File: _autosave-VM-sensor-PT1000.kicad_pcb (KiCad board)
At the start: 2 copper layers, 25.4 x 21.6 mm, 17 parts, among them P1 PT100, P2 ADC, P3 PWR, U1 AMS1117, U2 MCP6001

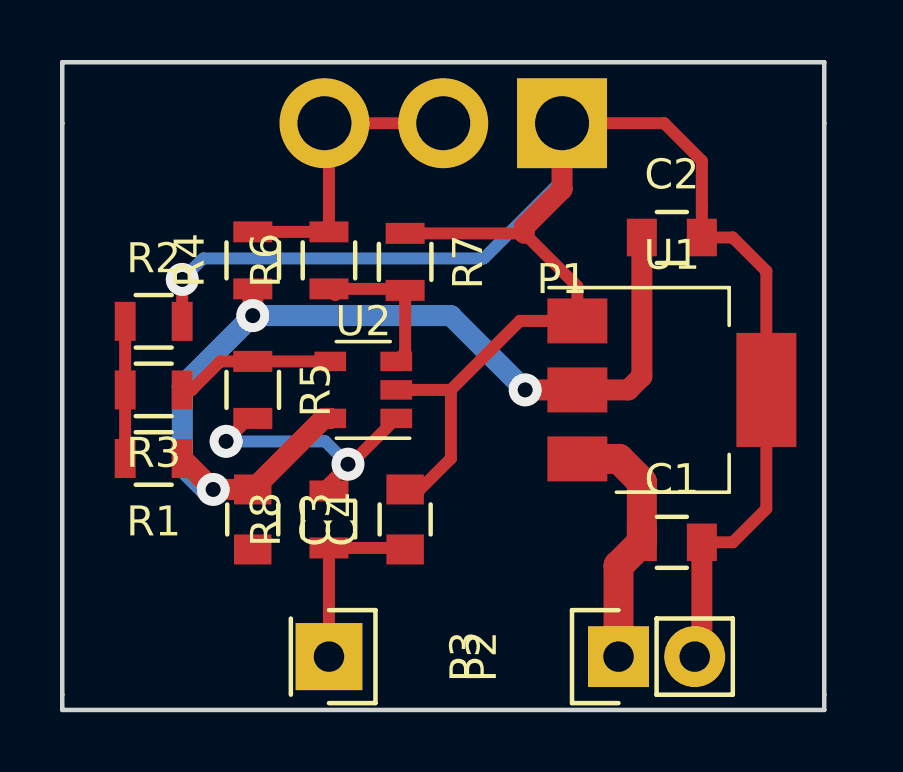
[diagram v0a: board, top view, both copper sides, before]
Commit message: change component 0603 to 0805 & header
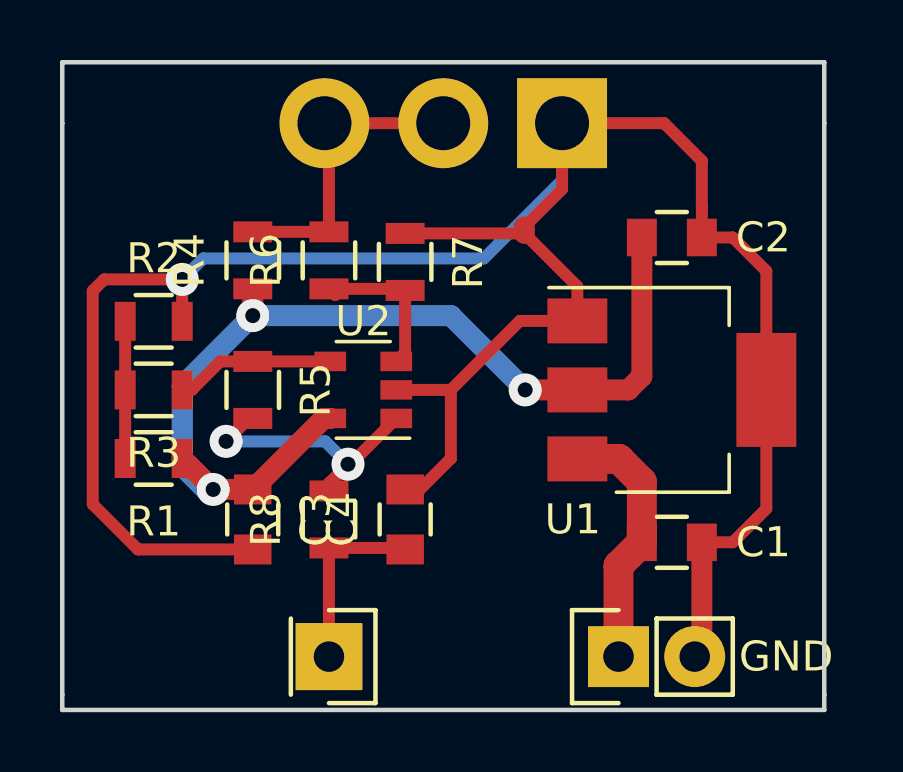
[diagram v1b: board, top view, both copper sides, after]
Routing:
- net GND: track 65.4 -> 81.6 mm
- added copper zone on B.Cu, net GND
- added copper zone on F.Cu, net GND
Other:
- board text added: "GND"
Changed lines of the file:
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@@
   (general
     (links 30)
-    (no_connects 5)
+    (no_connects 0)
     (area 114.224999 61.392999 139.775001 83.133001)
     (thickness 1.6)
-    (drawings 8)
-    (tracks 83)
+    (drawings 9)
+    (tracks 88)
     (zones 0)
     (modules 17)
@@
     (last_trace_width 0.4)
     (trace_clearance 0.2)
-    (zone_clearance 0.508)
+    (zone_clearance 0.4)
     (zone_45_only no)
     (trace_min 0.2)
@@
     (uvia_min_drill 0.1)
     (pcb_text_width 0.3)
-    (pcb_text_size 1.5 1.5)
+    (pcb_text_size 1 1)
     (mod_edge_width 0.15)
     (mod_text_size 1 1)
@@
     (descr "Hirose DF63 connector, DF63-3P-3.96DSA, 3.96mm pitch, top entry THT")
     (tags "connector hirose df63 vertical through hole")
-    (fp_text reference P1 (at 0 -5.2 180) (layer F.SilkS)
+    (fp_text reference P1 (at 0 -5.2 180) (layer F.SilkS) hide
       (effects (font (size 1 1) (thickness 0.15)))
     )
@@
     (tags "CMS SOT")
     (attr smd)
-    (fp_text reference U1 (at 0 -4.5) (layer F.SilkS)
+    (fp_text reference U1 (at -3.302 4.318) (layer F.SilkS)
       (effects (font (size 1 1) (thickness 0.15)))
     )
@@
     (tags "capacitor 0805")
     (attr smd)
-    (fp_text reference C1 (at 0 -2.1) (layer F.SilkS)
+    (fp_text reference C1 (at 3.048 0) (layer F.SilkS)
       (effects (font (size 1 1) (thickness 0.15)))
     )
@@
     (tags "capacitor 0805")
     (attr smd)
-    (fp_text reference C2 (at 0 -2.1) (layer F.SilkS)
+    (fp_text reference C2 (at 3.048 0) (layer F.SilkS)
       (effects (font (size 1 1) (thickness 0.15)))
     )
@@
     (descr "Through hole pin header")
     (tags "pin header")
-    (fp_text reference P3 (at 0 -5.1 90) (layer F.SilkS)
+    (fp_text reference P3 (at 0 -5.1 90) (layer F.SilkS) hide
       (effects (font (size 1 1) (thickness 0.15)))
     )
@@
     (descr "Through hole pin header")
     (tags "pin header")
-    (fp_text reference P2 (at 0 -5.1 270) (layer F.SilkS)
+    (fp_text reference P2 (at 0 -5.1 270) (layer F.SilkS) hide
       (effects (font (size 1 1) (thickness 0.15)))
     )
@@
       (rotate (xyz 0 0 90))
     )
+  )
+  (gr_text GND (at 138.43 81.28) (layer F.SilkS)
+    (effects (font (size 1 1) (thickness 0.25)))
   )
   (gr_line (start 139.7 61.468) (end 139.7 63.5) (layer Edge.Cuts) (width 0.15))
@@
   (segment (start 133.62 77.47) (end 132.842 78.248) (width 1) (layer F.Cu) (net 1))
   (segment (start 132.842 78.248) (end 132.842 81.28) (width 1) (layer F.Cu) (net 1))
+  (segment (start 120.65 77.708) (end 116.824 77.708) (width 0.4) (layer F.Cu) (net 2))
+  (segment (start 116.824 77.708) (end 115.316 76.2) (width 0.4) (layer F.Cu) (net 2))
+  (segment (start 115.316 76.2) (end 115.316 69.088) (width 0.4) (layer F.Cu) (net 2))
+  (segment (start 115.316 69.088) (end 115.697 68.707) (width 0.4) (layer F.Cu) (net 2))
+  (segment (start 115.697 68.707) (end 118.3005 68.707) (width 0.4) (layer F.Cu) (net 2))
   (segment (start 118.999 68.0085) (end 128.3515 68.0085) (width 0.4) (layer B.Cu) (net 2))
   (segment (start 128.3515 68.0085) (end 130.96 65.4) (width 0.4) (layer B.Cu) (net 2))
@@
   (segment (start 136.652 77.47) (end 137.77 76.352) (width 0.4) (layer F.Cu) (net 2))
   (segment (start 137.77 76.352) (end 137.77 72.39) (width 0.4) (layer F.Cu) (net 2))
-  (segment (start 130.96 63.5) (end 130.96 65.7) (width 0.7) (layer F.Cu) (net 2))
-  (segment (start 130.96 65.7) (end 129.7028 66.9572) (width 0.7) (layer F.Cu) (net 2))
+  (segment (start 130.96 63.5) (end 130.96 65.7) (width 0.4) (layer F.Cu) (net 2))
+  (segment (start 130.96 65.7) (end 129.7028 66.9572) (width 0.4) (layer F.Cu) (net 2))
   (segment (start 129.7028 66.9572) (end 129.7028 67.1728) (width 0.7) (layer F.Cu) (net 2))
   (segment (start 130.96 63.5) (end 134.366 63.5) (width 0.4) (layer F.Cu) (net 2))
@@
   (segment (start 123.19 69.022) (end 125.6792 69.022) (width 0.4) (layer F.Cu) (net 9))
   (segment (start 125.6792 69.022) (end 125.73 69.0728) (width 0.4) (layer F.Cu) (net 9))
+  (zone (net 2) (net_name GND) (layer F.Cu) (hatch edge 0.508)
+    (connect_pads (clearance 0.4))
+    (min_thickness 0.4)
+    (fill yes (arc_segments 32) (thermal_gap 0.508) (thermal_bridge_width 0.508))
+    (polygon
+      (pts
+        (xy 114.3 61.468) (xy 139.7 61.468) (xy 139.7 83.058) (xy 114.3 83.058)
+      )
+    )
+  )
+  (zone (net 2) (net_name GND) (layer B.Cu) (hatch edge 0.508)
+    (connect_pads (clearance 0.4))
+    (min_thickness 0.4)
+    (fill yes (arc_segments 32) (thermal_gap 0.508) (thermal_bridge_width 0.508))
+    (polygon
+      (pts
+        (xy 114.3 61.468) (xy 139.7 61.468) (xy 139.7 83.058) (xy 114.3 83.058)
+      )
+    )
+  )
 )
